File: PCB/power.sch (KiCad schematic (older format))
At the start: 42 parts

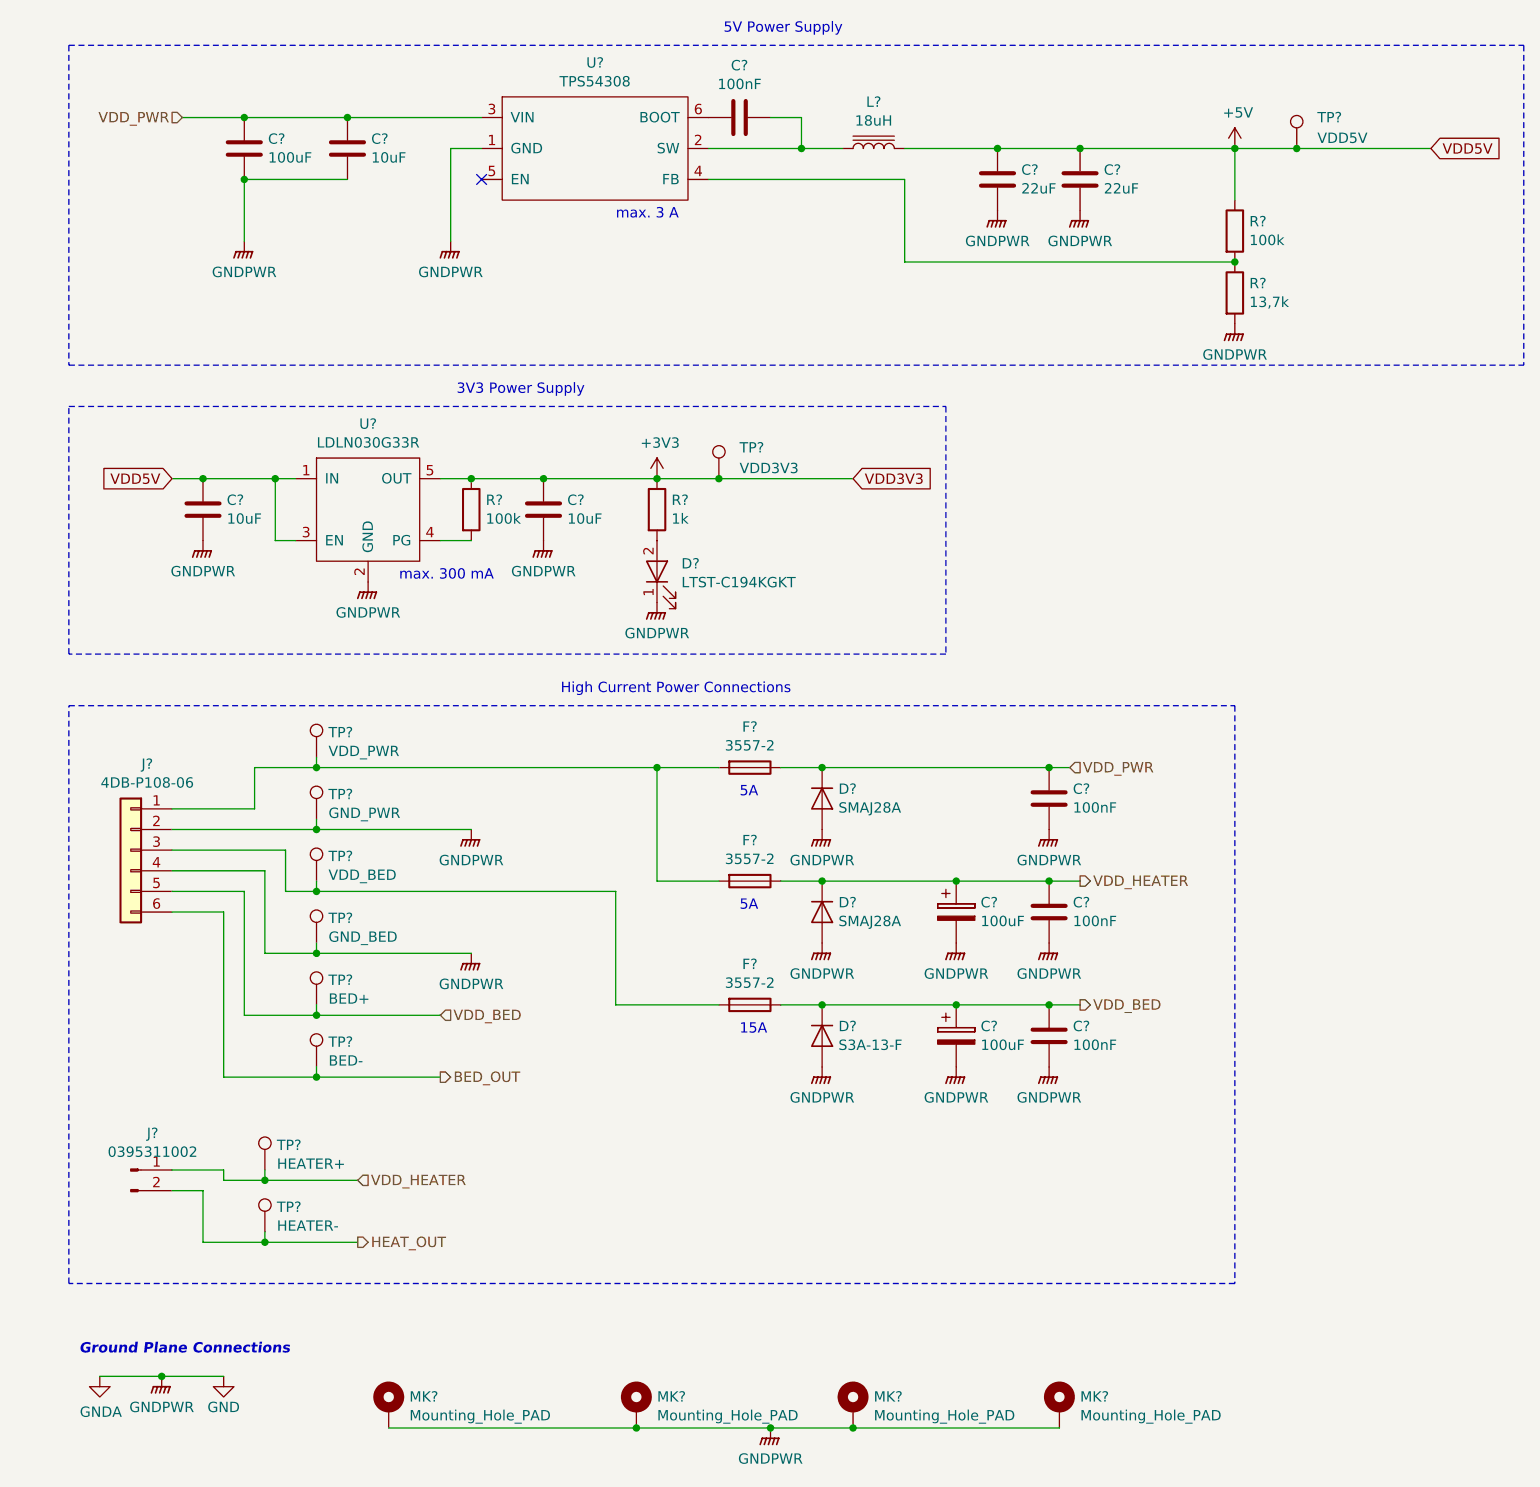
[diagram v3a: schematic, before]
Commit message: Fixed bugs found with ERC.
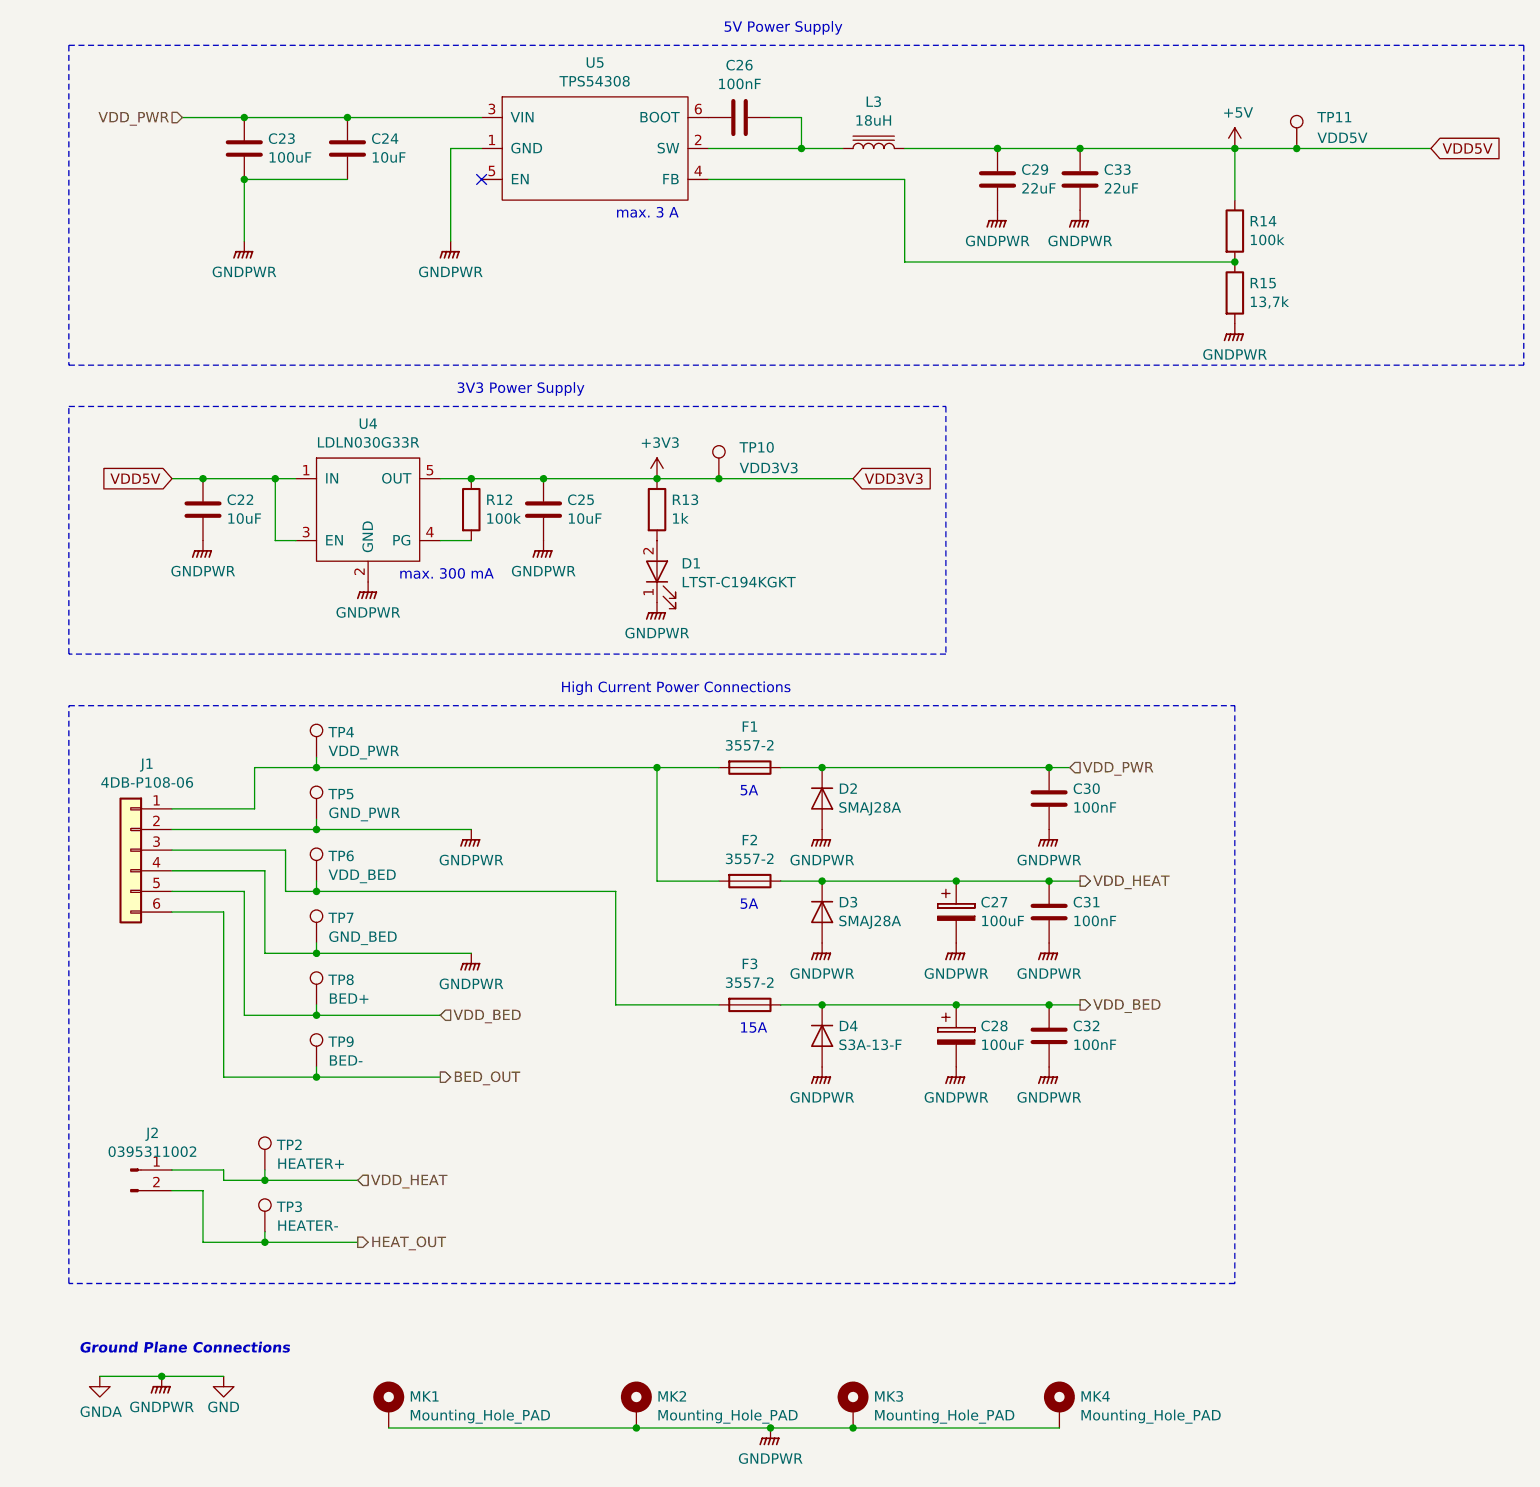
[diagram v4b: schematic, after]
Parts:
- gave numbers to parts that had none: 42
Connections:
- net VDD_HEATER renamed VDD_HEAT

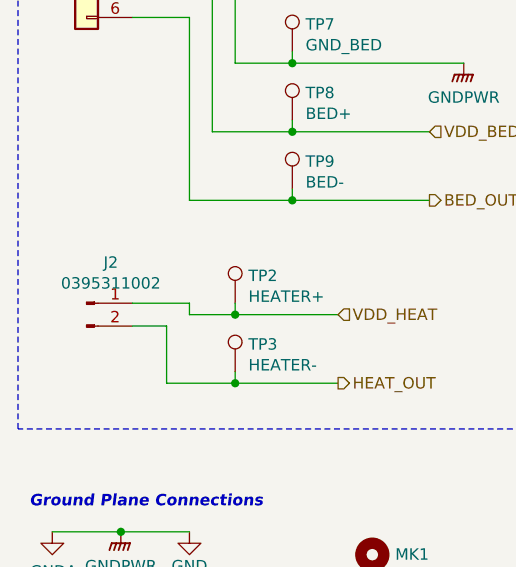
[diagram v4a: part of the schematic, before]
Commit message: Added missing foorprints.
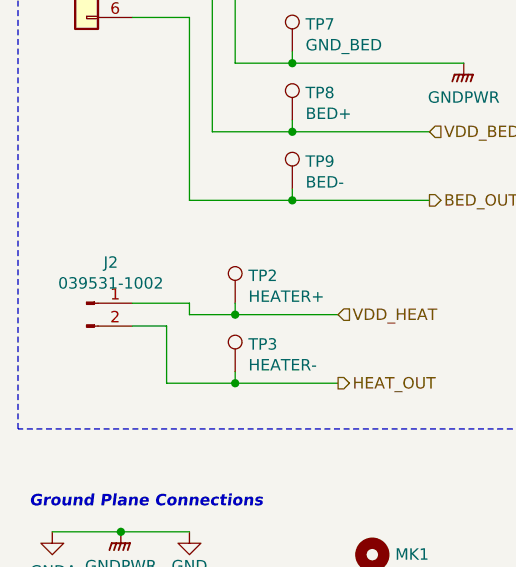
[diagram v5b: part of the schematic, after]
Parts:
- J2: value 0395311002 -> 039531-1002; footprint (none) -> custom-footprints:39531-1002
- U5: footprint (none) -> Package_TO_SOT_SMD:SOT-23-6
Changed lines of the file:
@@
 F 0 "U5" H 3250 1565 50  0000 C CNN
 F 1 "TPS54308" H 3250 1474 50  0000 C CNN
-F 2 "" H 3250 1150 50  0001 C CNN
-F 3 "" H 3250 1150 50  0001 C CNN
+F 2 "Package_TO_SOT_SMD:SOT-23-6" H 3250 1150 50  0001 C CNN
+F 3 "http://www.ti.com/lit/ds/symlink/tps54308.pdf" H 3250 1150 50  0001 C CNN
 	1    3250 1150
 	1    0    0    -1
@@
 P 1000 6100
 F 0 "J2" H 1106 6278 50  0000 C CNN
-F 1 "0395311002" H 1106 6187 50  0000 C CNN
-F 2 "" H 1000 6100 50  0001 C CNN
+F 1 "039531-1002" H 1106 6187 50  0000 C CNN
+F 2 "custom-footprints:39531-1002" H 1000 6100 50  0001 C CNN
 F 3 "~" H 1000 6100 50  0001 C CNN
 	1    1000 6100

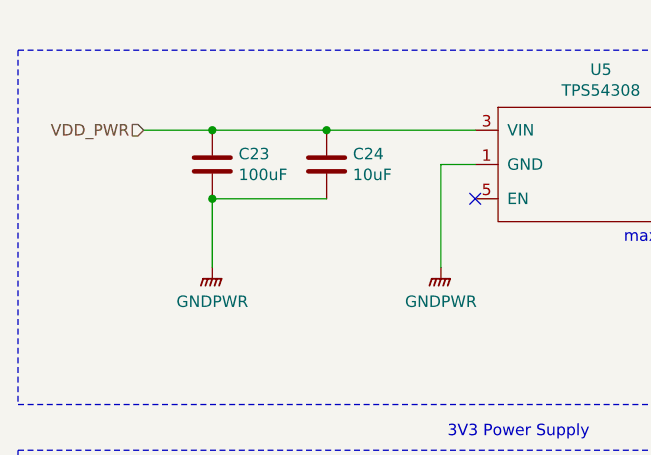
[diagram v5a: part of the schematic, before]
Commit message: Fixed annotations and assignment errors.
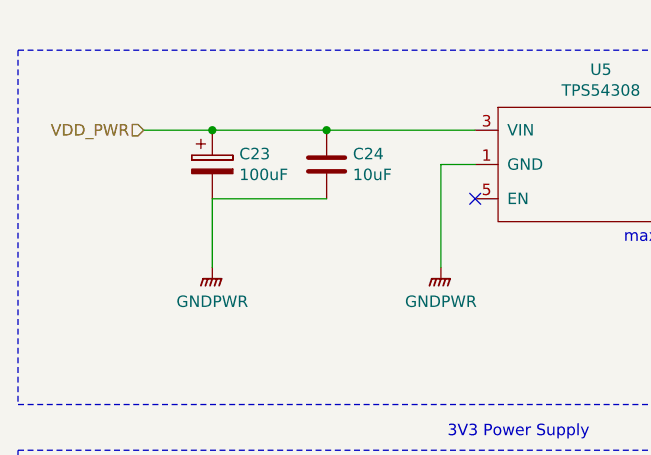
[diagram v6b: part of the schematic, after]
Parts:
- removed C23: 100uF, Capacitor_THT:CP_Radial_D6.3mm_P2.50mm, symbol Device:C
- added C23: 100uF, Capacitor_THT:CP_Radial_D6.3mm_P2.50mm, symbol Device:CP
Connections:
- net GND: now also C23.2
- net VDD_PWR: now also C23.1
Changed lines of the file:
@@
 	1    0    0    -1
 $EndComp
-Wire Wire Line
-	1250 1000 1550 1000
-$Comp
-L Device:C C23
-U 1 1 5AF61016
-P 1550 1150
-F 0 "C23" H 1665 1196 50  0000 L CNN
-F 1 "100uF" H 1665 1105 50  0000 L CNN
-F 2 "Capacitor_THT:CP_Radial_D6.3mm_P2.50mm" H 1588 1000 50  0001 C CNN
-F 3 "https://eu.mouser.com/datasheet/2/293/e-uvz-1219460.pdf" H 1550 1150 50  0001 C CNN
-F 4 "UVZ1V101MED" H 1550 1150 50  0001 C CNN "Mfr. No"
-	1    1550 1150
-	1    0    0    -1
-$EndComp
-Connection ~ 1550 1000
-Wire Wire Line
-	1550 1000 2050 1000
 $Comp
 L Device:C C24
@@
 Wire Wire Line
 	1550 1300 2050 1300
-Connection ~ 1550 1300
 $Comp
 L power:GNDPWR #PWR047
@@
 F 1 "100uF" H 5118 4805 50  0000 L CNN
 F 2 "Capacitor_THT:CP_Radial_D6.3mm_P2.50mm" H 5038 4700 50  0001 C CNN
-F 3 "https://www.mouser.de/ProductDetail/Wurth-Electronics/860010573007?qs=sGAEpiMZZMvwFf0viD3Y3aZipiehufnXDo3pM9Qdgp1gvK74JBMa%252bg%3d%3d" H 5000 4850 50  0001 C CNN
+F 3 "https://eu.mouser.com/datasheet/2/293/e-uvz-1219460.pdf" H 5000 4850 50  0001 C CNN
 	1    5000 4850
 	1    0    0    -1
@@
 F 1 "100nF" H 5565 5405 50  0000 L CNN
 F 2 "Capacitor_SMD:C_1812_4532Metric" H 5488 5300 50  0001 C CNN
-F 3 "https://www.mouser.de/ProductDetail/Wurth-Electronics/885012210025?qs=sGAEpiMZZMs0AnBnWHyRQEGbLOF2VP1iAfG0rM5y1N6W8Ylp3ErKJw%3d%3d" H 5450 5450 50  0001 C CNN
+F 3 "" H 5450 5450 50  0001 C CNN
 	1    5450 5450
 	1    0    0    -1
@@
 F 1 "100nF" H 5565 4805 50  0000 L CNN
 F 2 "Capacitor_SMD:C_1812_4532Metric" H 5488 4700 50  0001 C CNN
-F 3 "https://www.mouser.de/ProductDetail/Wurth-Electronics/885012210025?qs=sGAEpiMZZMs0AnBnWHyRQEGbLOF2VP1iAfG0rM5y1N6W8Ylp3ErKJw%3d%3d" H 5450 4850 50  0001 C CNN
+F 3 "" H 5450 4850 50  0001 C CNN
 	1    5450 4850
 	1    0    0    -1
@@
 F 1 "100nF" H 5565 4255 50  0000 L CNN
 F 2 "Capacitor_SMD:C_1812_4532Metric" H 5488 4150 50  0001 C CNN
-F 3 "https://www.mouser.de/ProductDetail/Wurth-Electronics/885012210025?qs=sGAEpiMZZMs0AnBnWHyRQEGbLOF2VP1iAfG0rM5y1N6W8Ylp3ErKJw%3d%3d" H 5450 4300 50  0001 C CNN
+F 3 "" H 5450 4300 50  0001 C CNN
 	1    5450 4300
 	1    0    0    -1
@@
 F 1 "100uF" H 5118 5405 50  0000 L CNN
 F 2 "Capacitor_THT:CP_Radial_D6.3mm_P2.50mm" H 5038 5300 50  0001 C CNN
-F 3 "https://www.mouser.de/ProductDetail/Wurth-Electronics/860010573007?qs=sGAEpiMZZMvwFf0viD3Y3aZipiehufnXDo3pM9Qdgp1gvK74JBMa%252bg%3d%3d" H 5000 5450 50  0001 C CNN
+F 3 "https://eu.mouser.com/datasheet/2/293/e-uvz-1219460.pdf" H 5000 5450 50  0001 C CNN
 	1    5000 5450
 	1    0    0    -1
@@
 	1    0    0    -1
 $EndComp
+Wire Wire Line
+	1250 1000 1550 1000
+$Comp
+L Device:CP C23
+U 1 1 5AFA3BBA
+P 1550 1150
+F 0 "C23" H 1668 1196 50  0000 L CNN
+F 1 "100uF" H 1668 1105 50  0000 L CNN
+F 2 "Capacitor_THT:CP_Radial_D6.3mm_P2.50mm" H 1588 1000 50  0001 C CNN
+F 3 "https://eu.mouser.com/datasheet/2/293/e-uvz-1219460.pdf" H 1550 1150 50  0001 C CNN
+	1    1550 1150
+	1    0    0    -1
+$EndComp
+Connection ~ 1550 1000
+Wire Wire Line
+	1550 1000 2050 1000
 $EndSCHEMATC
